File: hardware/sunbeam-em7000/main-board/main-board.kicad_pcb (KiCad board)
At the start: 4 copper layers, 131 x 125 mm, 455 parts, among them J101 TAB1_LINE1, J102 TAB2_LINE_IN, J103 TAB3_NEUTRAL_IN, J106 TAB6_COFVALVE, J107 TAB7_COFFPUMP, J108 TAB8_STEAMPUMP, J109 TAB9_HOTVALVE, J110 WB_RET, J401 SWD, J402 USB_PANEL, J501 TEMP_C, J502 TEMP_S, J503 TEMP_W, J520 FLOW, J521 STM_D, J522 BREW_D, J523 SPARE_A, J524 BREW_A, J525 SPARE_AN2_H, J570 CURR1_H, J571 CURR2_H, J620 PT1_H, J622 PT1_2W_P, J623 PT1_23W_N, J625 PT2_H, J627 PT2_2W_P, J628 PT2_23W_N, J630 WT1_H, J635 WT2_H, J761 WB_LV10, J791 SP2, J821 CON2, J861 KNOB, J862 REED, K201 HF115F-Q/005-1H, K731 HF32FA-G/005-HSL1, K741 HF32FA-G/005-HSL1, Q201 NX3008NBK, Q202 NX3008NBK, Q701 AO3400A, Q711 AO3400A, Q731 AO3400A, Q741 AO3400A, Q761 AO3400A, Q771 AO3400A, Q821 AO3400A, Q822 AO3401A, Q823 AO3400A, Q824 AO3400A, SW401 RESET, T701 BTA204S-600B, T711 BTA204S-600B, U201 74AHCT1G17, U301 IRM-20-5, U302 LT1963AEST-3.3#TRPBF, U401 STM32H743VIT6, U402 TLV803SDBZR, U520 SN74LVC1G17, U601 AMC131M02, U602 LTV-814S-TA1-A, U620 MAX31865ATP+, U621 MAX31865ATP+, U630 HX711, U631 HX711, U701 MOC3052SVM, U711 MOC3052SVM, U791 SN74HCT541PWR, Y401 8 MHz, Y402 32.768 kHz, Y601 8.000MHz

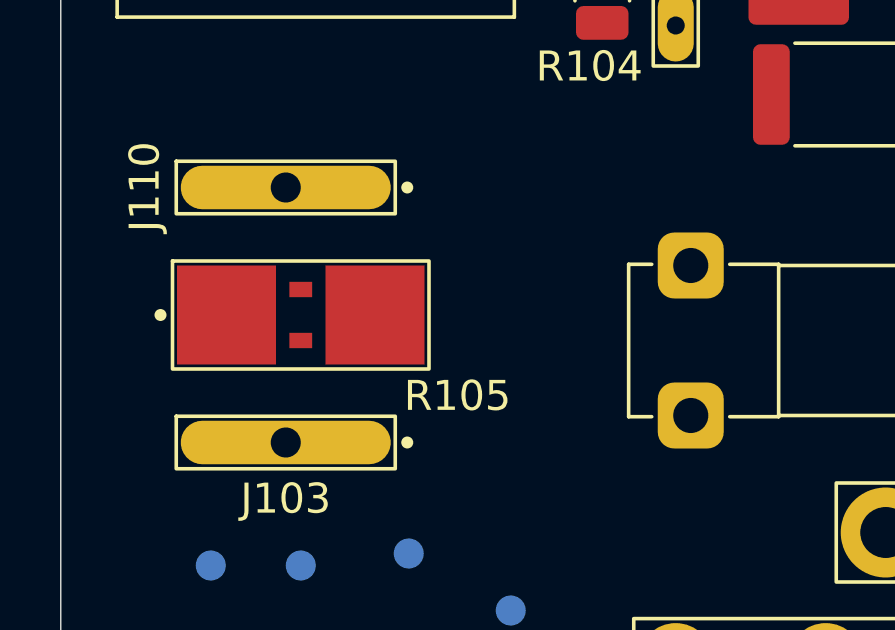
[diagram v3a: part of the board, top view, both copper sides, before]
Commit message: main-board: placement candidate 4 [SOL-HW-MAIN-BOARD-PROVEN-AND-LAID-OUT.C7]
Candidate 3 with the AMC_HGND net on the converter's high-side returns and the net tie NT601 appended at the shunt's neutral-side terminal.

Co-Authored-By: Claude Sonnet 5.5 <noreply@anthropic.com>
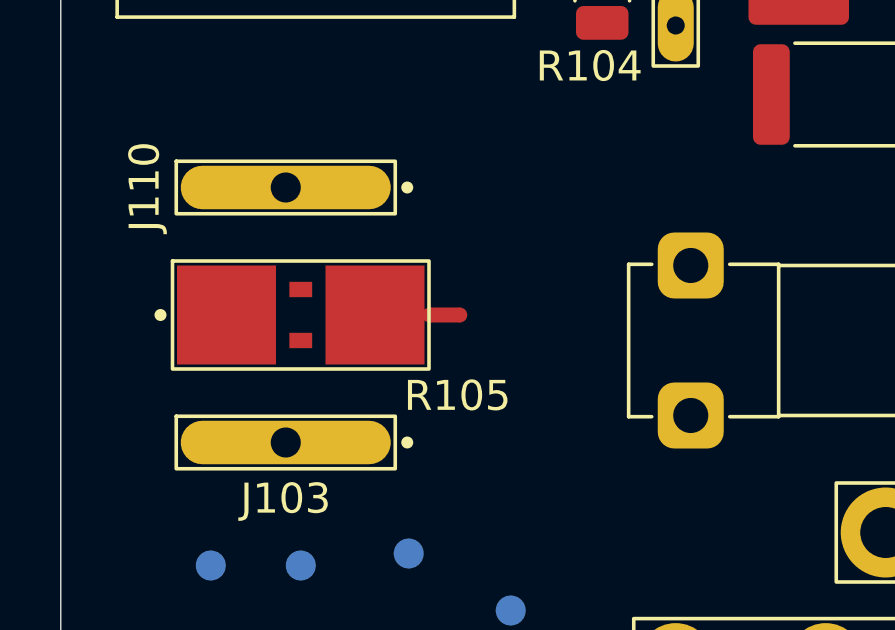
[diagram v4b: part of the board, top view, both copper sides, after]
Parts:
- added NT601: NetTie_2, NetTie:NetTie-2_SMD_Pad0.5mm, F.Cu at (13.8, 86.7)
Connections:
- C605 pad 2: /NEUTRAL -> /Supply voltage and current measurement/AMC_HGND
- C606 pad 2: /NEUTRAL -> /Supply voltage and current measurement/AMC_HGND
- C607 pad 2: /NEUTRAL -> /Supply voltage and current measurement/AMC_HGND
- C608 pad 2: /NEUTRAL -> /Supply voltage and current measurement/AMC_HGND
- F602 pad 2: /NEUTRAL -> /Supply voltage and current measurement/AMC_HGND
- R604 pad 2: /NEUTRAL -> /Supply voltage and current measurement/AMC_HGND
- R606 pad 2: /NEUTRAL -> /Supply voltage and current measurement/AMC_HGND
- U601 pad 5: /NEUTRAL -> /Supply voltage and current measurement/AMC_HGND
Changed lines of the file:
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@@
 			(size 2.1 0.6)
 			(layers "F.Cu" "F.Mask" "F.Paste")
-			(net "/NEUTRAL")
+			(net "/Supply voltage and current measurement/AMC_HGND")
 			(pinfunction "HGND_5")
 			(pintype "passive")
@@
 			(layers "F.Cu" "F.Mask" "F.Paste")
 			(roundrect_rratio 0.25)
-			(net "/NEUTRAL")
+			(net "/Supply voltage and current measurement/AMC_HGND")
 			(pintype "passive")
 		)
@@
 			(layers "F.Cu" "F.Mask" "F.Paste")
 			(roundrect_rratio 0.25)
-			(net "/NEUTRAL")
+			(net "/Supply voltage and current measurement/AMC_HGND")
 			(pintype "passive")
 		)
@@
 			(layers "F.Cu" "F.Mask" "F.Paste")
 			(roundrect_rratio 0.25)
-			(net "/NEUTRAL")
+			(net "/Supply voltage and current measurement/AMC_HGND")
 			(pintype "passive")
 		)
@@
 			(layers "F.Cu" "F.Mask" "F.Paste")
 			(roundrect_rratio 0.25)
-			(net "/NEUTRAL")
+			(net "/Supply voltage and current measurement/AMC_HGND")
 			(pintype "passive")
 		)
@@
 			(layers "F.Cu" "F.Mask" "F.Paste")
 			(roundrect_rratio 0.25)
-			(net "/NEUTRAL")
+			(net "/Supply voltage and current measurement/AMC_HGND")
 			(pintype "passive")
 		)
@@
 			(layers "F.Cu" "F.Mask" "F.Paste")
 			(roundrect_rratio 0.217391)
-			(net "/NEUTRAL")
+			(net "/Supply voltage and current measurement/AMC_HGND")
 			(pintype "passive")
 		)
@@
 		)
 	)
+	(footprint "NetTie:NetTie-2_SMD_Pad0.5mm"
+		(layer "F.Cu")
+		(at 13.8 86.65)
+		(descr "Net tie, 2 pin, 0.5mm square SMD pads")
+		(tags "net tie")
+		(property "Reference" "NT601"
+			(at 0 -1.2 0)
+			(layer "F.SilkS")
+			(hide yes)
+			(effects
+				(font
+					(size 1 1)
+					(thickness 0.15)
+				)
+			)
+		)
+		(property "Value" "NetTie_2"
+			(at 0 1.2 0)
+			(layer "F.Fab")
+			(hide yes)
+			(effects
+				(font
+					(size 1 1)
+					(thickness 0.15)
+				)
+			)
+		)
+		(property "Datasheet" ""
+			(at 0 0 0)
+			(unlocked yes)
+			(layer "F.Fab")
+			(hide yes)
+			(effects
+				(font
+					(size 1.27 1.27)
+					(thickness 0.15)
+				)
+			)
+		)
+		(property "Description" "Net tie, 2 pins"
+			(at 0 0 0)
+			(unlocked yes)
+			(layer "F.Fab")
+			(hide yes)
+			(effects
+				(font
+					(size 1.27 1.27)
+					(thickness 0.15)
+				)
+			)
+		)
+		(attr exclude_from_pos_files exclude_from_bom allow_missing_courtyard)
+		(net_tie_pad_groups "1, 2")
+		(duplicate_pad_numbers_are_jumpers no)
+		(fp_poly
+			(pts
+				(xy -0.5 -0.25) (xy 0.5 -0.25) (xy 0.5 0.25) (xy -0.5 0.25)
+			)
+			(stroke
+				(width 0)
+				(type solid)
+			)
+			(fill yes)
+			(layer "F.Cu")
+		)
+		(pad "1" smd circle
+			(at -0.5 0)
+			(size 0.5 0.5)
+			(layers "F.Cu")
+			(net "/NEUTRAL")
+			(pintype "passive")
+		)
+		(pad "2" smd circle
+			(at 0.5 0)
+			(size 0.5 0.5)
+			(layers "F.Cu")
+			(net "/Supply voltage and current measurement/AMC_HGND")
+			(pintype "passive")
+		)
+		(embedded_fonts no)
+	)
 	(footprint "Package_TO_SOT_SMD:SOT-23"
 		(layer "F.Cu")
@@
 			(layers "F.Cu" "F.Mask" "F.Paste")
 			(roundrect_rratio 0.25)
-			(net "/NEUTRAL")
+			(net "/Supply voltage and current measurement/AMC_HGND")
 			(pintype "passive")
 		)

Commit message: main-board: mains copper [SOL-HW-MAIN-BOARD-PROVEN-AND-LAID-OUT.C7]
Co-Authored-By: Claude Sonnet 5.5 <noreply@anthropic.com>
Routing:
- net /Valve drives/VALVE_COM: track 0.00 -> 140.1 mm
- net /Supply voltage and current measurement/AMC_HGND: track 0.00 -> 68.5 mm, vias 0 -> 7
- net /SHUNT_SENSE_NEUTRAL: track 0.00 -> 58.4 mm, vias 0 -> 4
- net /SHUNT_SENSE_IN: track 0.00 -> 53.6 mm, vias 0 -> 2
- net /COFVALVE: track 0.00 -> 44.3 mm, vias 0 -> 1
- net /HOTVALVE: track 0.00 -> 43.2 mm, vias 0 -> 1
- net /Zero-crossing detector/ZC_LED_A: track 0.00 -> 39.8 mm, vias 0 -> 2
- net /Supply voltage and current measurement/VMEAS_DIV: track 0.00 -> 39.6 mm, vias 0 -> 3
- net /Pump drives/PUMP_C_OPTO_MT: track 0.00 -> 36.6 mm, vias 0 -> 2
- net /Pump drives/PUMP_S_SNUB: track 0.00 -> 30.6 mm
- net /Supply voltage and current measurement/AMC_AIN1P: track 0.00 -> 30.1 mm, vias 0 -> 2
- net /Pump drives/PUMP_S_OPTO_MT: track 0.00 -> 28.3 mm, vias 0 -> 2
- net /Pump drives/PUMP_C_SNUB: track 0.00 -> 21.1 mm, vias 0 -> 1
- net /Supply voltage and current measurement/AMC_DCDC_HGND: track 0.00 -> 20.0 mm, vias 0 -> 2
- net /Logic supply/LINE_MOD: track 0.00 -> 17.5 mm
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- added copper zone on B.Cu, net /LINE
- added copper zone on F.Cu, net /LINE
- added copper zone on In2.Cu, net /LINE
- added copper zone on B.Cu, net /Mains entry and load feed/LINE_F
- added copper zone on B.Cu, net /Mains entry and load feed/NEUTRAL_IN
- added copper zone on F.Cu, net /Mains entry and load feed/NEUTRAL_IN
- added copper zone on B.Cu, net /NEUTRAL
- added copper zone on F.Cu, net /NEUTRAL
- added copper zone on In2.Cu, net /NEUTRAL
- added copper zone on In1.Cu, net GND
- added copper zone on In2.Cu, net GND
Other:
- outline, holes or cut-outs redrawn
